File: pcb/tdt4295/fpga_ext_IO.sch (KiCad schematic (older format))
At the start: 44 parts, among them J301 618015330923, J302 Conn_02x08_Odd_Even, U301 NUP4114UCW1T2G, U302 NUP4114UCW1T2G, U303 NUP4114UCW1T2G, U304 NUP4114UCW1T2G

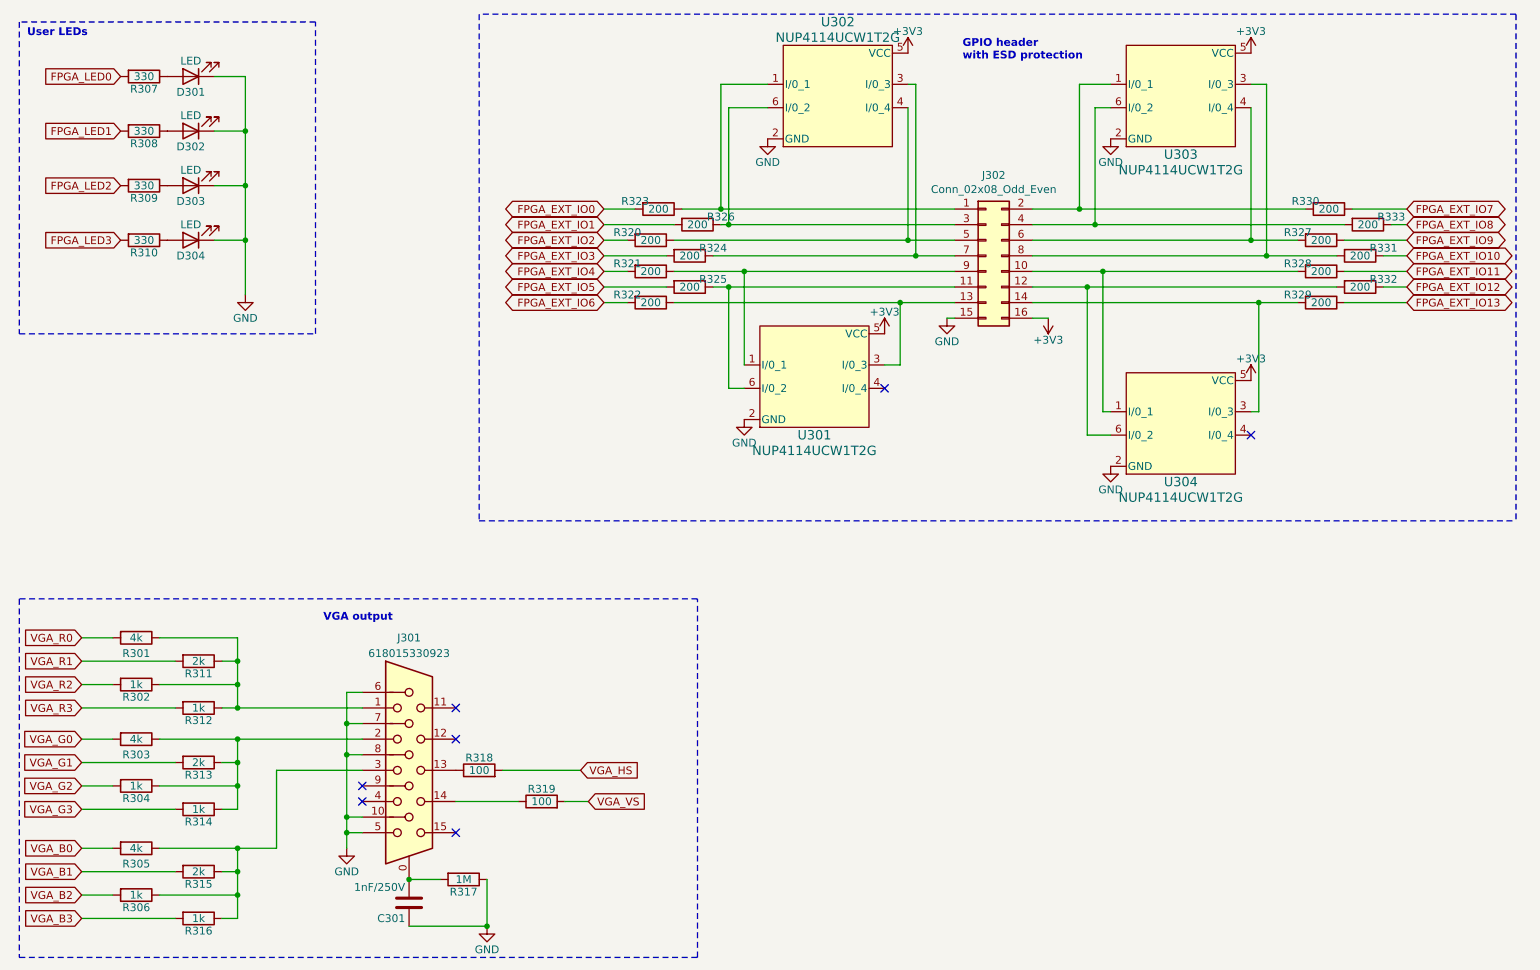
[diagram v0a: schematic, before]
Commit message: associate (some) footprints to the symbols
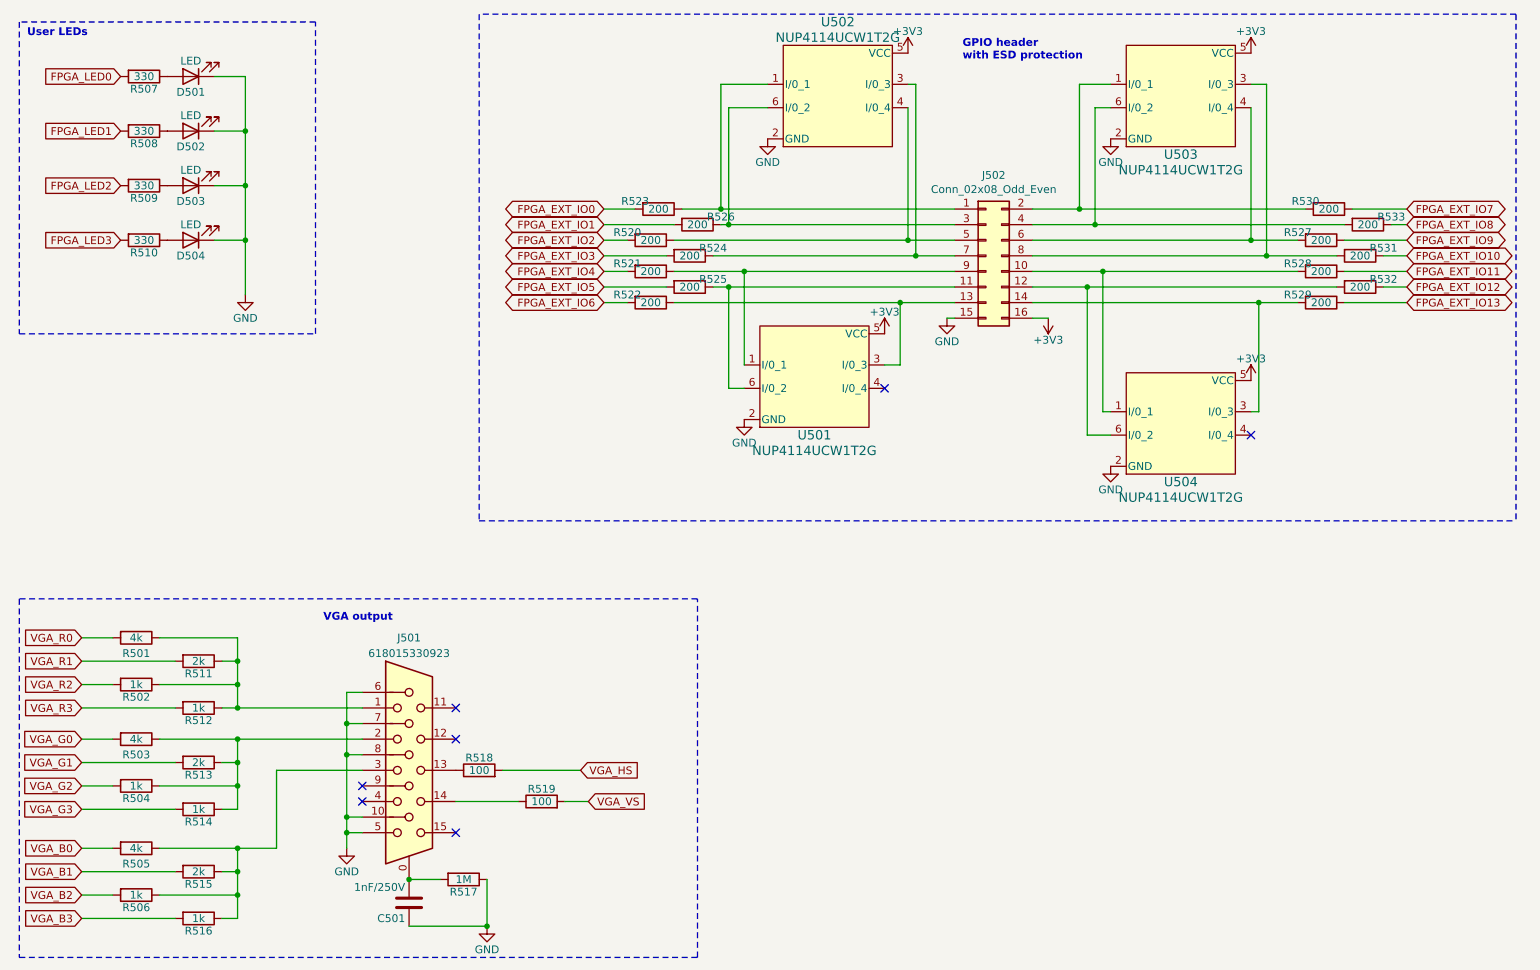
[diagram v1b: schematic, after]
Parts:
- R501: renamed from R301; DK_Detail_Page (none) -> https://no.farnell.com/koa-speer-electronics/rn73r2bttd4001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
- R502: renamed from R302; DK_Detail_Page (none) -> https://www.digikey.no/product-detail/no/susumu/RR0510P-102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
- R503: renamed from R303; DK_Detail_Page (none) -> https://no.farnell.com/koa-speer-electronics/rn73r2bttd4001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
- R504: renamed from R304; DK_Detail_Page (none) -> https://www.digikey.no/product-detail/no/susumu/RR0510P-102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
- R505: renamed from R305; DK_Detail_Page (none) -> https://no.farnell.com/koa-speer-electronics/rn73r2bttd4001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
- R506: renamed from R306; DK_Detail_Page (none) -> https://www.digikey.no/product-detail/no/susumu/RR0510P-102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
- R507: renamed from R307; DK_Detail_Page (none) -> https://www.digikey.no/product-detail/no/koa-speer-electron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
- R508: renamed from R308; DK_Detail_Page (none) -> https://www.digikey.no/product-detail/no/koa-speer-electron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
- R509: renamed from R309; DK_Detail_Page (none) -> https://www.digikey.no/product-detail/no/koa-speer-electron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
- R510: renamed from R310; DK_Detail_Page (none) -> https://www.digikey.no/product-detail/no/koa-speer-electron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
- R511: renamed from R311; DK_Detail_Page (none) -> https://www.digikey.no/product-detail/no/yageo/RC1206FR-072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
- R512: renamed from R312; DK_Detail_Page (none) -> https://www.digikey.no/product-detail/no/susumu/RR0510P-102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
- R513: renamed from R313; DK_Detail_Page (none) -> https://www.digikey.no/product-detail/no/yageo/RC1206FR-072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
- R514: renamed from R314; DK_Detail_Page (none) -> https://www.digikey.no/product-detail/no/susumu/RR0510P-102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
- R515: renamed from R315; DK_Detail_Page (none) -> https://www.digikey.no/product-detail/no/yageo/RC1206FR-072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
- R516: renamed from R316; DK_Detail_Page (none) -> https://www.digikey.no/product-detail/no/susumu/RR0510P-102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
- R517: renamed from R317; DK_Detail_Page (none) -> https://www.digikey.no/product-detail/no/panasonic-electron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
- R518: renamed from R318; DK_Detail_Page (none) -> https://www.digikey.no/product-detail/no/vishay-dale/TNPW08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
- R519: renamed from R319; DK_Detail_Page (none) -> https://www.digikey.no/product-detail/no/vishay-dale/TNPW08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
- R520: renamed from R320; DK_Detail_Page (none) -> https://www.digikey.no/product-detail/no/stackpole-electron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
- R521: renamed from R321; DK_Detail_Page (none) -> https://www.digikey.no/product-detail/no/stackpole-electron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
- R522: renamed from R322; DK_Detail_Page (none) -> https://www.digikey.no/product-detail/no/stackpole-electron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
- R523: renamed from R323; DK_Detail_Page (none) -> https://www.digikey.no/product-detail/no/stackpole-electron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
- R524: renamed from R324; DK_Detail_Page (none) -> https://www.digikey.no/product-detail/no/stackpole-electron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
- R525: renamed from R325; DK_Detail_Page (none) -> https://www.digikey.no/product-detail/no/stackpole-electron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
- R526: renamed from R326; DK_Detail_Page (none) -> https://www.digikey.no/product-detail/no/stackpole-electron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
- R527: renamed from R327; DK_Detail_Page (none) -> https://www.digikey.no/product-detail/no/stackpole-electron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
- R528: renamed from R328; DK_Detail_Page (none) -> https://www.digikey.no/product-detail/no/stackpole-electron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
- R529: renamed from R329; DK_Detail_Page (none) -> https://www.digikey.no/product-detail/no/stackpole-electron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
- R530: renamed from R330; DK_Detail_Page (none) -> https://www.digikey.no/product-detail/no/stackpole-electron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
- R531: renamed from R331; DK_Detail_Page (none) -> https://www.digikey.no/product-detail/no/stackpole-electron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
- R532: renamed from R332; DK_Detail_Page (none) -> https://www.digikey.no/product-detail/no/stackpole-electron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
- R533: renamed from R333; DK_Detail_Page (none) -> https://www.digikey.no/product-detail/no/stackpole-electron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
- renumbered C301 to C501, D301 to D501, D302 to D502, D303 to D503, D304 to D504, J301 to J501, J302 to J502, U301 to U501, U302 to U502, U303 to U503, U304 to U504

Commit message: pcb: Added some more footprints/part numbers
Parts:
- R520, R521, R522, R523, R524, R525, R526, R527, R528, R529, R530, R531, R532, R533: footprint Resistor_SMD:R_0805_2012Metric_Pad1.20x1.40mm_HandSolder -> Resistor_SMD:R_2512_6332Metric_Pad1.40x3.35mm_HandSolder; Component name RNCF0805TKY200R -> 3521200RFT; DK_Detail_Page https://www.digikey.no/product-detail/no/stackpole-electron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 -> https://www.digikey.no/product-detail/en/te-connectivity-pa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

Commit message: pcb: correct vga circuit, modify resistor/capacitor sizes
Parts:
- R502, R504, R506: footprint Resistor_SMD:R_0402_1005Metric_Pad0.72x0.64mm_HandSolder -> Resistor_SMD:R_0805_2012Metric_Pad1.20x1.40mm_HandSolder; DK_Detail_Page https://www.digikey.no/product-detail/no/susumu/RR0510P-102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 -> https://www.digikey.no/product-detail/en/susumu/RR1220P-102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
- R512, R514, R516: value 1k -> 510; footprint Resistor_SMD:R_0402_1005Metric_Pad0.72x0.64mm_HandSolder -> Resistor_SMD:R_0805_2012Metric_Pad1.20x1.40mm_HandSolder; Component name RR0510P-102-D -> ERA-6AED511V; DK_Detail_Page https://www.digikey.no/product-detail/no/susumu/RR0510P-102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 -> https://www.digikey.no/product-detail/en/panasonic-electron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
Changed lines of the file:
@@
 F 0 "R502" V 1380 4800 50  0000 C CNN
 F 1 "1k" V 1300 4800 50  0000 C CNN
-F 2 "Resistor_SMD:R_0402_1005Metric_Pad0.72x0.64mm_HandSolder" V 1230 4800 50  0001 C CNN
+F 2 "Resistor_SMD:R_0805_2012Metric_Pad1.20x1.40mm_HandSolder" V 1230 4800 50  0001 C CNN
 F 3 "https://www.susumu.co.jp/common/pdf/n_catalog_partition05_en.pdf" H 1300 4800 50  0001 C CNN
 F 4 "RR0510P-102-D" H 1300 4800 50  0001 C CNN "Component name"
-F 5 "https://www.digikey.no/product-detail/no/susumu/RR0510P-102-D/RR05P1-0KDCT-ND/432937" H 1300 4800 50  0001 C CNN "DK_Detail_Page"
+F 5 "https://www.digikey.no/product-detail/en/susumu/RR1220P-102-D/RR12P1-0KDCT-ND/432830" H 1300 4800 50  0001 C CNN "DK_Detail_Page"
 	1    1300 4800
-	0    1    1    0
-$EndComp
-$Comp
-L Device:R R512
-U 1 1 615B6041
-P 1700 4950
-F 0 "R512" V 1780 4950 50  0000 C CNN
-F 1 "1k" V 1700 4950 50  0000 C CNN
-F 2 "Resistor_SMD:R_0402_1005Metric_Pad0.72x0.64mm_HandSolder" V 1630 4950 50  0001 C CNN
-F 3 "https://www.susumu.co.jp/common/pdf/n_catalog_partition05_en.pdf" H 1700 4950 50  0001 C CNN
-F 4 "RR0510P-102-D" H 1700 4950 50  0001 C CNN "Component name"
-F 5 "https://www.digikey.no/product-detail/no/susumu/RR0510P-102-D/RR05P1-0KDCT-ND/432937" H 1700 4950 50  0001 C CNN "DK_Detail_Page"
-	1    1700 4950
 	0    1    1    0
 $EndComp
@@
 Wire Wire Line
 	950  4800 1150 4800
-Wire Wire Line
-	1450 4800 1950 4800
 Wire Wire Line
 	950  4950 1550 4950
@@
 F 0 "R504" V 1380 5450 50  0000 C CNN
 F 1 "1k" V 1300 5450 50  0000 C CNN
-F 2 "Resistor_SMD:R_0402_1005Metric_Pad0.72x0.64mm_HandSolder" V 1230 5450 50  0001 C CNN
+F 2 "Resistor_SMD:R_0805_2012Metric_Pad1.20x1.40mm_HandSolder" V 1230 5450 50  0001 C CNN
 F 3 "https://www.susumu.co.jp/common/pdf/n_catalog_partition05_en.pdf" H 1300 5450 50  0001 C CNN
 F 4 "RR0510P-102-D" H 1300 5450 50  0001 C CNN "Component name"
-F 5 "https://www.digikey.no/product-detail/no/susumu/RR0510P-102-D/RR05P1-0KDCT-ND/432937" H 1300 5450 50  0001 C CNN "DK_Detail_Page"
+F 5 "https://www.digikey.no/product-detail/en/susumu/RR1220P-102-D/RR12P1-0KDCT-ND/432830" H 1300 5450 50  0001 C CNN "DK_Detail_Page"
 	1    1300 5450
 	0    1    1    0
@@
 P 1700 5600
 F 0 "R514" V 1780 5600 50  0000 C CNN
-F 1 "1k" V 1700 5600 50  0000 C CNN
-F 2 "Resistor_SMD:R_0402_1005Metric_Pad0.72x0.64mm_HandSolder" V 1630 5600 50  0001 C CNN
-F 3 "https://www.susumu.co.jp/common/pdf/n_catalog_partition05_en.pdf" H 1700 5600 50  0001 C CNN
-F 4 "RR0510P-102-D" H 1700 5600 50  0001 C CNN "Component name"
-F 5 "https://www.digikey.no/product-detail/no/susumu/RR0510P-102-D/RR05P1-0KDCT-ND/432937" H 1700 5600 50  0001 C CNN "DK_Detail_Page"
+F 1 "510" V 1700 5600 50  0000 C CNN
+F 2 "Resistor_SMD:R_0805_2012Metric_Pad1.20x1.40mm_HandSolder" V 1630 5600 50  0001 C CNN
+F 3 "" H 1700 5600 50  0001 C CNN
+F 4 "ERA-6AED511V" H 1700 5600 50  0001 C CNN "Component name"
+F 5 "https://www.digikey.no/product-detail/en/panasonic-electronic-components/ERA-6AED511V/P123855CT-ND/9467784" H 1700 5600 50  0001 C CNN "DK_Detail_Page"
 	1    1700 5600
 	0    1    1    0
@@
 F 0 "R506" V 1380 6150 50  0000 C CNN
 F 1 "1k" V 1300 6150 50  0000 C CNN
-F 2 "Resistor_SMD:R_0402_1005Metric_Pad0.72x0.64mm_HandSolder" V 1230 6150 50  0001 C CNN
+F 2 "Resistor_SMD:R_0805_2012Metric_Pad1.20x1.40mm_HandSolder" V 1230 6150 50  0001 C CNN
 F 3 "https://www.susumu.co.jp/common/pdf/n_catalog_partition05_en.pdf" H 1300 6150 50  0001 C CNN
 F 4 "RR0510P-102-D" H 1300 6150 50  0001 C CNN "Component name"
-F 5 "https://www.digikey.no/product-detail/no/susumu/RR0510P-102-D/RR05P1-0KDCT-ND/432937" H 1300 6150 50  0001 C CNN "DK_Detail_Page"
+F 5 "https://www.digikey.no/product-detail/en/susumu/RR1220P-102-D/RR12P1-0KDCT-ND/432830" H 1300 6150 50  0001 C CNN "DK_Detail_Page"
 	1    1300 6150
 	0    1    1    0
@@
 P 1700 6300
 F 0 "R516" V 1780 6300 50  0000 C CNN
-F 1 "1k" V 1700 6300 50  0000 C CNN
-F 2 "Resistor_SMD:R_0402_1005Metric_Pad0.72x0.64mm_HandSolder" V 1630 6300 50  0001 C CNN
-F 3 "https://www.susumu.co.jp/common/pdf/n_catalog_partition05_en.pdf" H 1700 6300 50  0001 C CNN
-F 4 "RR0510P-102-D" H 1700 6300 50  0001 C CNN "Component name"
-F 5 "https://www.digikey.no/product-detail/no/susumu/RR0510P-102-D/RR05P1-0KDCT-ND/432937" H 1700 6300 50  0001 C CNN "DK_Detail_Page"
+F 1 "510" V 1700 6300 50  0000 C CNN
+F 2 "Resistor_SMD:R_0805_2012Metric_Pad1.20x1.40mm_HandSolder" V 1630 6300 50  0001 C CNN
+F 3 "" H 1700 6300 50  0001 C CNN
+F 4 "ERA-6AED511V" H 1700 6300 50  0001 C CNN "Component name"
+F 5 "https://www.digikey.no/product-detail/en/panasonic-electronic-components/ERA-6AED511V/P123855CT-ND/9467784" H 1700 6300 50  0001 C CNN "DK_Detail_Page"
 	1    1700 6300
 	0    1    1    0
@@
 Wire Wire Line
 	8550 2050 9000 2050
+Wire Wire Line
+	1450 4800 1950 4800
+$Comp
+L Device:R R512
+U 1 1 615B6041
+P 1700 4950
+F 0 "R512" V 1780 4950 50  0000 C CNN
+F 1 "510" V 1700 4950 50  0000 C CNN
+F 2 "Resistor_SMD:R_0805_2012Metric_Pad1.20x1.40mm_HandSolder" V 1630 4950 50  0001 C CNN
+F 3 "" H 1700 4950 50  0001 C CNN
+F 4 "ERA-6AED511V" H 1700 4950 50  0001 C CNN "Component name"
+F 5 "https://www.digikey.no/product-detail/en/panasonic-electronic-components/ERA-6AED511V/P123855CT-ND/9467784" H 1700 4950 50  0001 C CNN "DK_Detail_Page"
+	1    1700 4950
+	0    1    1    0
+$EndComp
 $EndSCHEMATC

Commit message: add footprints, rename components
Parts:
- C501: DK_Detail_Page (none) -> https://www.digikey.no/product-detail/en/w%C3%BCrth-elektro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
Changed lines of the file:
@@
 F 3 "~" H 3050 6200 50  0001 C CNN
 F 4 "8853522100131" H 3050 6200 50  0001 C CNN "Component name"
+F 5 "https://www.digikey.no/product-detail/en/w%C3%BCrth-elektronik/8853522100131/732-8853522100131CT-ND/6140854" H 3050 6200 50  0001 C CNN "DK_Detail_Page"
 	1    3050 6200
 	-1   0    0    1

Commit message: footprints for everything
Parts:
- D501, D502, D503, D504: footprint Diode_SMD:D_0805_2012Metric_Pad1.15x1.40mm_HandSolder -> LED_SMD:LED_0805_2012Metric_Pad1.15x1.40mm_HandSolder
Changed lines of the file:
@@
 F 0 "D502" H 1650 1350 50  0000 C CNN
 F 1 "LED" H 1650 1150 50  0000 C CNN
-F 2 "Diode_SMD:D_0805_2012Metric_Pad1.15x1.40mm_HandSolder" H 1650 1250 50  0001 C CNN
+F 2 "LED_SMD:LED_0805_2012Metric_Pad1.15x1.40mm_HandSolder" H 1650 1250 50  0001 C CNN
 F 3 "~" H 1650 1250 50  0001 C CNN
 	1    1650 1250
@@
 F 0 "D501" H 1650 1000 50  0000 C CNN
 F 1 "LED" H 1650 800 50  0000 C CNN
-F 2 "Diode_SMD:D_0805_2012Metric_Pad1.15x1.40mm_HandSolder" H 1650 900 50  0001 C CNN
+F 2 "LED_SMD:LED_0805_2012Metric_Pad1.15x1.40mm_HandSolder" H 1650 900 50  0001 C CNN
 F 3 "~" H 1650 900 50  0001 C CNN
 	1    1650 900
@@
 F 0 "D503" H 1650 1700 50  0000 C CNN
 F 1 "LED" H 1650 1500 50  0000 C CNN
-F 2 "Diode_SMD:D_0805_2012Metric_Pad1.15x1.40mm_HandSolder" H 1650 1600 50  0001 C CNN
+F 2 "LED_SMD:LED_0805_2012Metric_Pad1.15x1.40mm_HandSolder" H 1650 1600 50  0001 C CNN
 F 3 "~" H 1650 1600 50  0001 C CNN
 	1    1650 1600
@@
 F 0 "D504" H 1650 2050 50  0000 C CNN
 F 1 "LED" H 1650 1850 50  0000 C CNN
-F 2 "Diode_SMD:D_0805_2012Metric_Pad1.15x1.40mm_HandSolder" H 1650 1950 50  0001 C CNN
+F 2 "LED_SMD:LED_0805_2012Metric_Pad1.15x1.40mm_HandSolder" H 1650 1950 50  0001 C CNN
 F 3 "~" H 1650 1950 50  0001 C CNN
 	1    1650 1950

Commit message: associate component links with (almost) every component
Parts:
- D501, D502, D503, D504: footprint LED_SMD:LED_0805_2012Metric_Pad1.15x1.40mm_HandSolder -> LED_SMD:LED_1206_3216Metric_Pad1.42x1.75mm_HandSolder; Component name (none) -> 150120BS75000; DK_Detail_Page (none) -> https://www.digikey.no/product-detail/no/w%C3%BCrth-elektro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
- J501: Component name (none) -> 618015330923; DK_Detail_Page (none) -> https://www.digikey.no/products/no?keywords=618015330923
- J502: value Conn_02x08_Odd_Even -> FPGA GPIO; footprint Connector_PinHeader_2.54mm:PinHeader_2x08_P2.54mm_Vertical -> Connector_PinHeader_2.54mm:PinHeader_2x08_P2.54mm_Vertical_SMD; Component name (none) -> 0015910160; DK_Detail_Page (none) -> https://www.digikey.no/product-detail/en/molex/0015910160/W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
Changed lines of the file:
@@
 P 6750 2050
 F 0 "J502" H 6800 2567 50  0000 C CNN
-F 1 "Conn_02x08_Odd_Even" H 6800 2476 50  0000 C CNN
-F 2 "Connector_PinHeader_2.54mm:PinHeader_2x08_P2.54mm_Vertical" H 6750 2050 50  0001 C CNN
+F 1 "FPGA GPIO" H 6800 2476 50  0000 C CNN
+F 2 "Connector_PinHeader_2.54mm:PinHeader_2x08_P2.54mm_Vertical_SMD" H 6750 2050 50  0001 C CNN
 F 3 "~" H 6750 2050 50  0001 C CNN
+F 4 "0015910160" H 6750 2050 50  0001 C CNN "Component name"
+F 5 "https://www.digikey.no/product-detail/en/molex/0015910160/WM17462-ND/614778" H 6750 2050 50  0001 C CNN "DK_Detail_Page"
 	1    6750 2050
 	1    0    0    -1
@@
 F 0 "D502" H 1650 1350 50  0000 C CNN
 F 1 "LED" H 1650 1150 50  0000 C CNN
-F 2 "LED_SMD:LED_0805_2012Metric_Pad1.15x1.40mm_HandSolder" H 1650 1250 50  0001 C CNN
+F 2 "LED_SMD:LED_1206_3216Metric_Pad1.42x1.75mm_HandSolder" H 1650 1250 50  0001 C CNN
 F 3 "~" H 1650 1250 50  0001 C CNN
+F 4 "150120BS75000" H 1650 1250 50  0001 C CNN "Component name"
+F 5 "https://www.digikey.no/product-detail/no/w%C3%BCrth-elektronik/150120BS75000/732-4989-1-ND/4489931" H 1650 1250 50  0001 C CNN "DK_Detail_Page"
 	1    1650 1250
 	-1   0    0    1
@@
 F 0 "D501" H 1650 1000 50  0000 C CNN
 F 1 "LED" H 1650 800 50  0000 C CNN
-F 2 "LED_SMD:LED_0805_2012Metric_Pad1.15x1.40mm_HandSolder" H 1650 900 50  0001 C CNN
+F 2 "LED_SMD:LED_1206_3216Metric_Pad1.42x1.75mm_HandSolder" H 1650 900 50  0001 C CNN
 F 3 "~" H 1650 900 50  0001 C CNN
+F 4 "150120BS75000" H 1650 900 50  0001 C CNN "Component name"
+F 5 "https://www.digikey.no/product-detail/no/w%C3%BCrth-elektronik/150120BS75000/732-4989-1-ND/4489931" H 1650 900 50  0001 C CNN "DK_Detail_Page"
 	1    1650 900
 	-1   0    0    1
@@
 F 0 "D503" H 1650 1700 50  0000 C CNN
 F 1 "LED" H 1650 1500 50  0000 C CNN
-F 2 "LED_SMD:LED_0805_2012Metric_Pad1.15x1.40mm_HandSolder" H 1650 1600 50  0001 C CNN
+F 2 "LED_SMD:LED_1206_3216Metric_Pad1.42x1.75mm_HandSolder" H 1650 1600 50  0001 C CNN
 F 3 "~" H 1650 1600 50  0001 C CNN
+F 4 "150120BS75000" H 1650 1600 50  0001 C CNN "Component name"
+F 5 "https://www.digikey.no/product-detail/no/w%C3%BCrth-elektronik/150120BS75000/732-4989-1-ND/4489931" H 1650 1600 50  0001 C CNN "DK_Detail_Page"
 	1    1650 1600
 	-1   0    0    1
@@
 F 0 "D504" H 1650 2050 50  0000 C CNN
 F 1 "LED" H 1650 1850 50  0000 C CNN
-F 2 "LED_SMD:LED_0805_2012Metric_Pad1.15x1.40mm_HandSolder" H 1650 1950 50  0001 C CNN
+F 2 "LED_SMD:LED_1206_3216Metric_Pad1.42x1.75mm_HandSolder" H 1650 1950 50  0001 C CNN
 F 3 "~" H 1650 1950 50  0001 C CNN
+F 4 "150120BS75000" H 1650 1950 50  0001 C CNN "Component name"
+F 5 "https://www.digikey.no/product-detail/no/w%C3%BCrth-elektronik/150120BS75000/732-4989-1-ND/4489931" H 1650 1950 50  0001 C CNN "DK_Detail_Page"
 	1    1650 1950
 	-1   0    0    1
@@
 F 2 "VGA_618015330923-footprint:618015330923" H 2100 5750 50  0001 C CNN
 F 3 " ~" H 2100 5750 50  0001 C CNN
+F 4 "618015330923" H 3050 5350 50  0001 C CNN "Component name"
+F 5 "https://www.digikey.no/products/no?keywords=618015330923" H 3050 5350 50  0001 C CNN "DK_Detail_Page"
 	1    3050 5350
 	1    0    0    -1

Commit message: minor fixes and import everything into the router
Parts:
- J501: symbol Connector:DB15_Female_HighDensity_MountingHoles -> tdt4295:DB15_Female_HighDensity_MountingHoles
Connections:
- net at C501.2, R517.2: now also J501.SHELL, J501.SHELL1; no longer J501.0
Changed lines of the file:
@@
 	10150 500  10150 3750
 $Comp
-L Connector:DB15_Female_HighDensity_MountingHoles J501
+L tdt4295:DB15_Female_HighDensity_MountingHoles J501
 U 1 1 61509FEE
 P 3050 5350
